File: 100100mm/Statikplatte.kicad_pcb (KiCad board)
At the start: 2 copper layers, 100 x 100 mm, 32 parts, among them J1 VIN, J10 HV, J2 GND, J3 GND, J4 GND, J5 GND, J6 GND, J7 HV, J8 HV, J9 HV

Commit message: updated boards
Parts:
- removed G***: LOGO, otter:otter_small1
- D1, D10, D2, D3, D4, D5, D6, D7, D8, D9: value D -> SS34
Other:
- board text added: "Electrostatic adhesion plate Design by Jana Marie Hemsing"
- board text removed: "Electrostatic adhesion plate Design by Jan Henrik Hemsing"

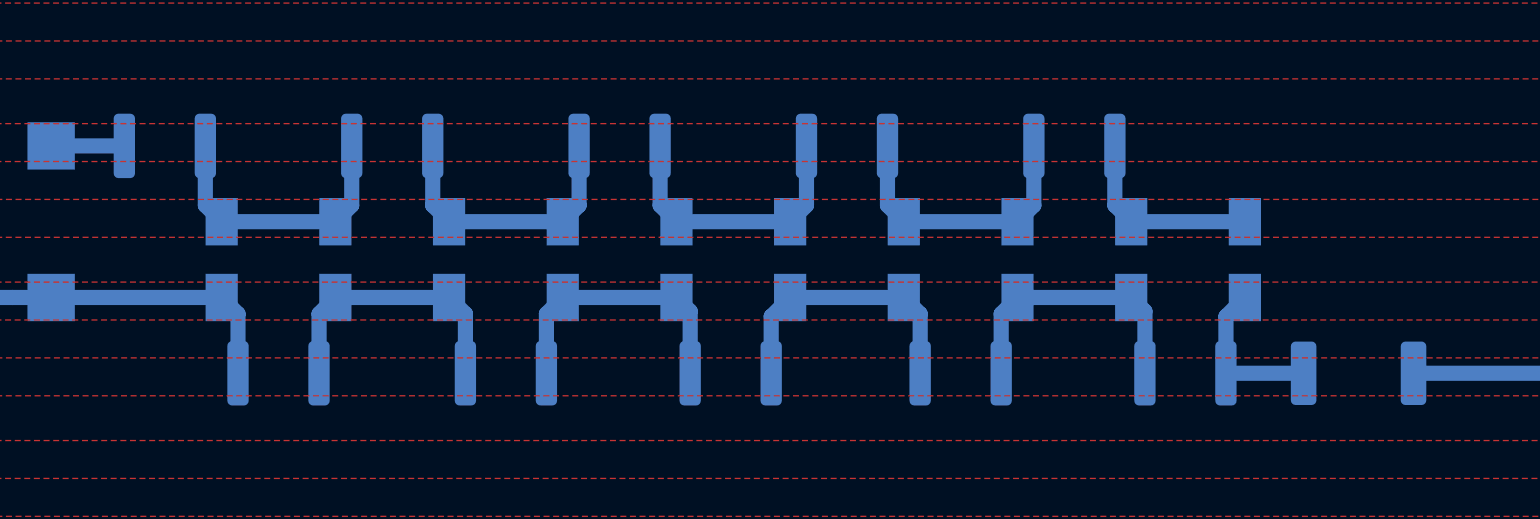
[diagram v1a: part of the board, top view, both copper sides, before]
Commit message: updated to KICAD 6
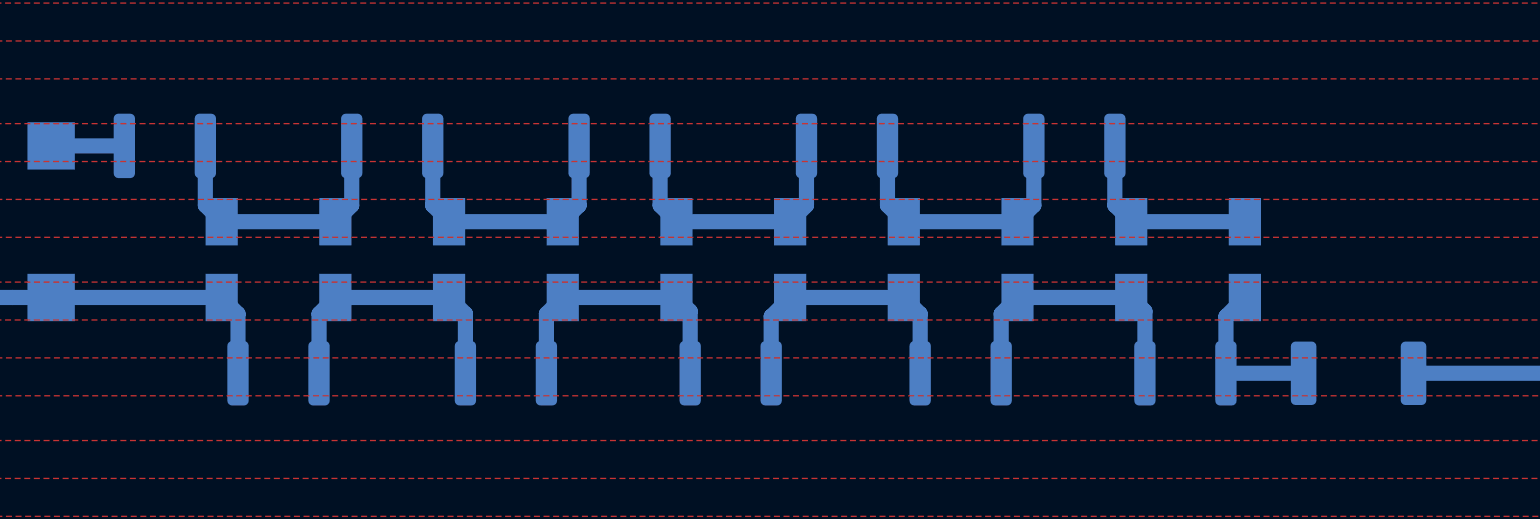
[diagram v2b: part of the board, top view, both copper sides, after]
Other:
- net class Default removed
